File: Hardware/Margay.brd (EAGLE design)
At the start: 50.2 x 30.4 mm, 71 parts, among them IC1 ATMEGA644M, J1 CONN_42.54_SCREW, J2 CONN_6SCREW_2.54, Q1 FDN360P, Q2 DMG3404, Q3 2N7002, Q4 FDN360P, Q6 FDN360P, U2 FT231X-Q

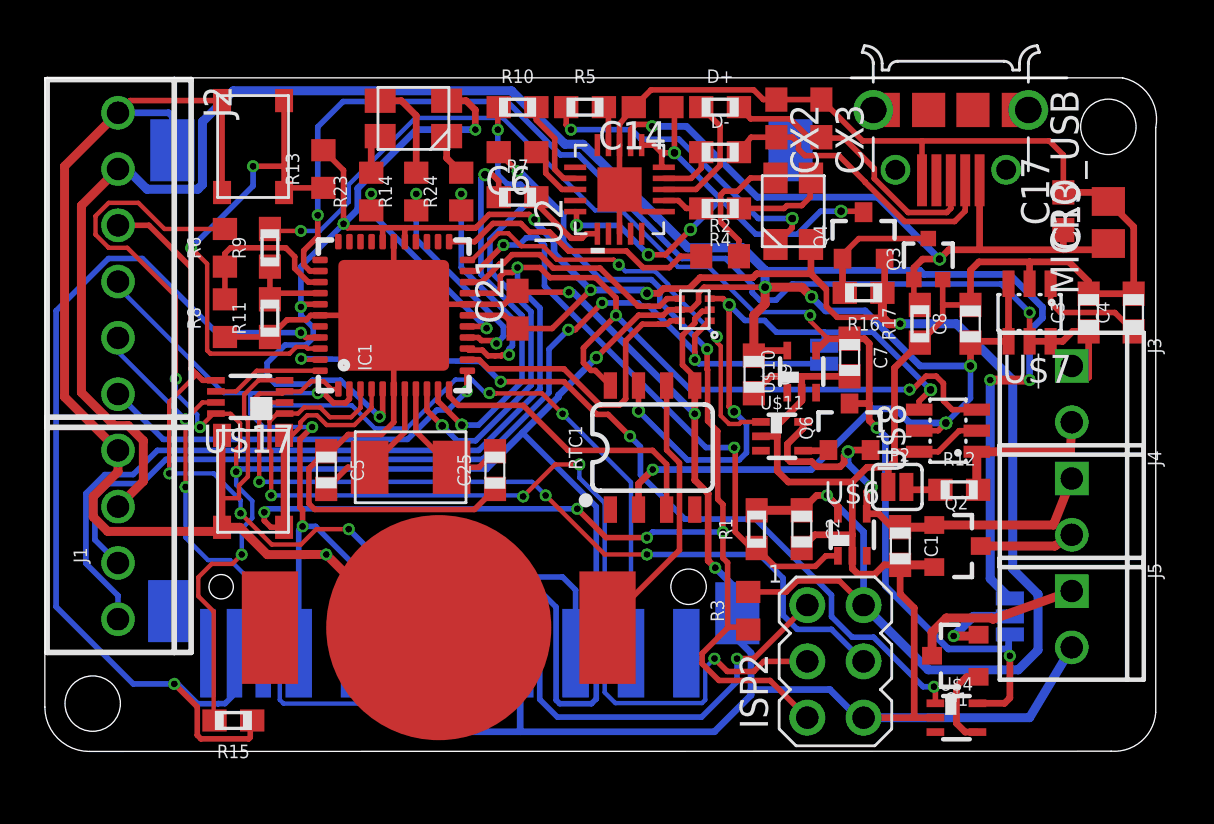
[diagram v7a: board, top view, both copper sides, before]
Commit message: Updated board to account for part changes
Fixed issue where 2x1 connectors displaced, also updated passives to new sizes
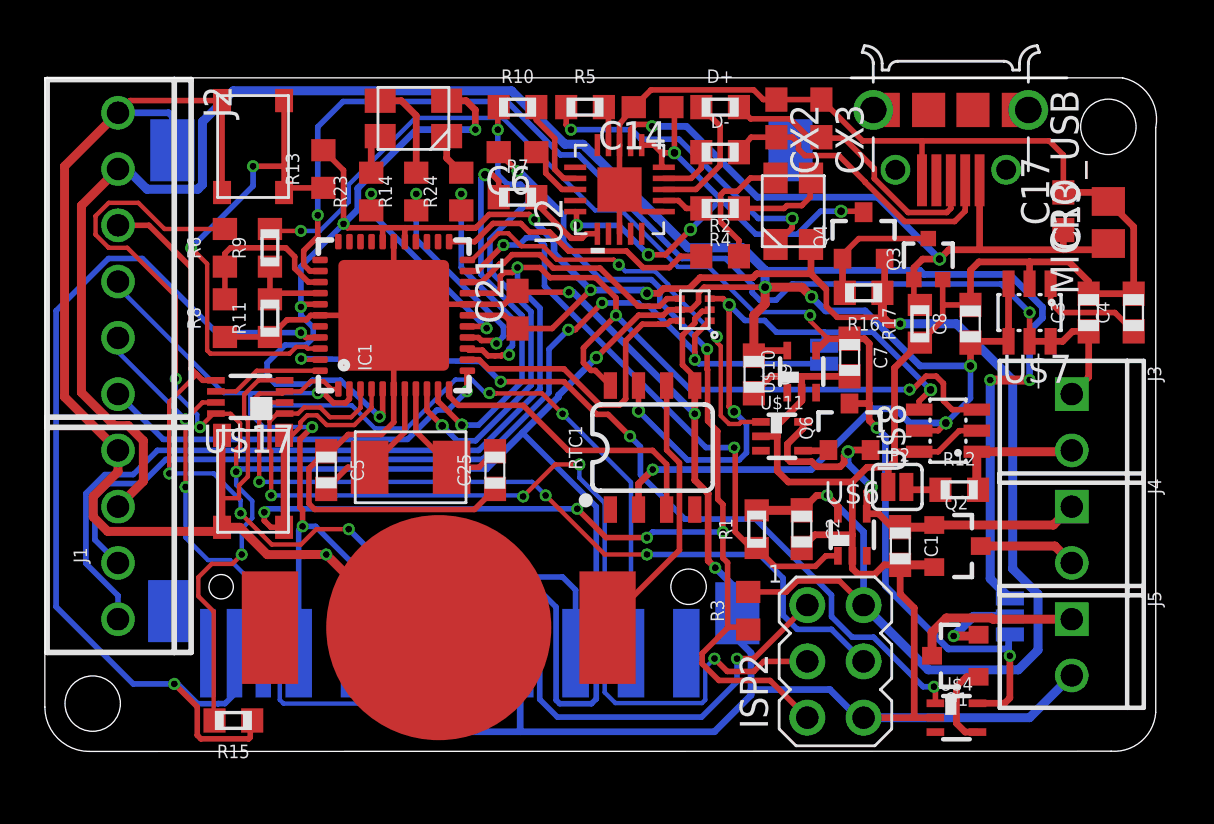
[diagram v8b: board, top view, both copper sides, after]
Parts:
- moved J3 1.27 mm to (46.4, 14.9)
- moved J5 1.27 mm to (46.4, 4.70)
- moved J4 1.27 mm to (46.4, 9.78)
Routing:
- net A0: track 7.30 -> 6.05 mm
- net VBAT+: track 20.9 -> 19.8 mm
- net GND: track 283.6 -> 282.6 mm
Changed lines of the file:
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@@
 <?xml version="1.0" encoding="utf-8"?>
 <!DOCTYPE eagle SYSTEM "eagle.dtd">
-<eagle version="8.5.1">
+<eagle version="9.0.1">
 <drawing>
 <settings>
@@
 <attribute name="MPN" value="OSTVN06A150" x="3.302" y="22.479" size="1.778" layer="27" rot="R270" display="off"/>
 </element>
-<element name="J3" library="bschulz" package="1X02_2.54_SCREWTERM" value="" x="46.355" y="16.129" rot="R270">
-<attribute name="DIGIKEY" value="ED10561-ND" x="46.355" y="16.129" size="1.778" layer="27" rot="R270" display="off"/>
-<attribute name="MF" value="OnShore" x="46.355" y="16.129" size="1.778" layer="27" rot="R270" display="off"/>
-<attribute name="MPN" value="OSTVN02A150" x="46.355" y="16.129" size="1.778" layer="27" rot="R270" display="off"/>
-</element>
-<element name="J4" library="bschulz" package="1X02_2.54_SCREWTERM" value="" x="46.355" y="11.049" rot="R270">
-<attribute name="DIGIKEY" value="ED10561-ND" x="46.355" y="11.049" size="1.778" layer="27" rot="R270" display="off"/>
-<attribute name="MF" value="OnShore" x="46.355" y="11.049" size="1.778" layer="27" rot="R270" display="off"/>
-<attribute name="MPN" value="OSTVN02A150" x="46.355" y="11.049" size="1.778" layer="27" rot="R270" display="off"/>
-</element>
-<element name="J5" library="bschulz" package="1X02_2.54_SCREWTERM" value="" x="46.355" y="5.969" rot="R270">
-<attribute name="DIGIKEY" value="ED10561-ND" x="46.355" y="5.969" size="1.778" layer="27" rot="R270" display="off"/>
-<attribute name="MF" value="OnShore" x="46.355" y="5.969" size="1.778" layer="27" rot="R270" display="off"/>
-<attribute name="MPN" value="OSTVN02A150" x="46.355" y="5.969" size="1.778" layer="27" rot="R270" display="off"/>
+<element name="J3" library="bschulz" package="1X02_2.54_SCREWTERM" value="" x="46.355" y="14.859" rot="R270">
+<attribute name="DIGIKEY" value="ED10561-ND" x="46.355" y="14.859" size="1.778" layer="27" rot="R270" display="off"/>
+<attribute name="MF" value="OnShore" x="46.355" y="14.859" size="1.778" layer="27" rot="R270" display="off"/>
+<attribute name="MPN" value="OSTVN02A150" x="46.355" y="14.859" size="1.778" layer="27" rot="R270" display="off"/>
+</element>
+<element name="J4" library="bschulz" package="1X02_2.54_SCREWTERM" value="" x="46.355" y="9.779" rot="R270">
+<attribute name="DIGIKEY" value="ED10561-ND" x="46.355" y="9.779" size="1.778" layer="27" rot="R270" display="off"/>
+<attribute name="MF" value="OnShore" x="46.355" y="9.779" size="1.778" layer="27" rot="R270" display="off"/>
+<attribute name="MPN" value="OSTVN02A150" x="46.355" y="9.779" size="1.778" layer="27" rot="R270" display="off"/>
+</element>
+<element name="J5" library="bschulz" package="1X02_2.54_SCREWTERM" value="" x="46.355" y="4.699" rot="R270">
+<attribute name="DIGIKEY" value="ED10561-ND" x="46.355" y="4.699" size="1.778" layer="27" rot="R270" display="off"/>
+<attribute name="MF" value="OnShore" x="46.355" y="4.699" size="1.778" layer="27" rot="R270" display="off"/>
+<attribute name="MPN" value="OSTVN02A150" x="46.355" y="4.699" size="1.778" layer="27" rot="R270" display="off"/>
 </element>
 <element name="JP1" library="SparkFun-Jumpers" library_urn="urn:adsk.eagle:library:528" package="SMT-JUMPER_3_1-NC_PASTE_SILK" package3d_urn="urn:adsk.eagle:package:39293/1" value="JUMPER-SMT_3_1-NC_PASTE_SILK" x="43.561" y="6.096" rot="MR270"/>
@@
 <wire x1="36.449" y1="9.779" x2="36.449" y2="12.16115" width="0.3048" layer="1"/>
 <wire x1="38.0746" y1="12.827" x2="38.0746" y2="11.938" width="0.3048" layer="1"/>
-<wire x1="46.355" y1="4.699" x2="44.45" y2="1.524" width="0.4064" layer="16"/>
+<wire x1="46.355" y1="3.429" x2="44.45" y2="1.524" width="0.4064" layer="16"/>
 <wire x1="44.45" y1="1.524" x2="36.957" y2="1.524" width="0.4064" layer="16"/>
 <wire x1="49.403" y1="20.916" x2="49.149" y2="20.662" width="0.254" layer="1"/>
@@
 <wire x1="40.048" y1="10.121" x2="38.608" y2="10.121" width="0.4064" layer="1"/>
 <wire x1="40.3424" y1="10.0266" x2="40.148" y2="10.221" width="0.4064" layer="1"/>
-<wire x1="46.355" y1="12.319" x2="45.527" y2="10.221" width="0.4064" layer="1"/>
+<wire x1="46.355" y1="11.049" x2="45.527" y2="10.221" width="0.4064" layer="1"/>
 <wire x1="45.527" y1="10.221" x2="40.148" y2="10.221" width="0.4064" layer="1"/>
 <contactref element="U$11" pad="5"/>
@@
 <wire x1="40.048" y1="4.318" x2="40.048" y2="5.377" width="0.4064" layer="1"/>
 <wire x1="42.74529375" y1="6.0236" x2="42.79989375" y2="5.969" width="0.4064" layer="1"/>
-<wire x1="42.79989375" y1="5.969" x2="46.355" y2="7.239" width="0.4064" layer="1"/>
+<wire x1="42.79989375" y1="5.969" x2="46.355" y2="5.969" width="0.4064" layer="1"/>
 <wire x1="40.048" y1="5.377" x2="40.6946" y2="6.0236" width="0.4064" layer="1"/>
 <wire x1="40.6946" y1="6.0236" x2="42.74529375" y2="6.0236" width="0.4064" layer="1"/>
@@
 <wire x1="44.45" y1="19.812" x2="43.1602" y2="21.1018" width="0.254" layer="16"/>
 <wire x1="43.1602" y1="21.1018" x2="33.734375" y2="21.1018" width="0.254" layer="16"/>
-<wire x1="46.355" y1="17.399" x2="47.117" y2="16.891" width="0.3048" layer="1"/>
+<wire x1="46.355" y1="16.129" x2="47.117" y2="16.891" width="0.3048" layer="1"/>
 <wire x1="47.117" y1="16.891" x2="47.117" y2="18.962" width="0.3048" layer="1"/>
 <wire x1="45.4" y1="18.512" x2="45.944" y2="18.512" width="0.3048" layer="1"/>
@@
 <wire x1="42.067" y1="11.869" x2="42.125" y2="11.811" width="0.4064" layer="1"/>
 <wire x1="42.067" y1="13.528" x2="46.294" y2="13.528" width="0.4064" layer="1"/>
-<wire x1="46.294" y1="13.528" x2="46.355" y2="14.859" width="0.4064" layer="1"/>
+<wire x1="46.294" y1="13.528" x2="46.355" y2="13.589" width="0.4064" layer="1"/>
 </signal>
 <signal name="VBAT-">
 <contactref element="Q2" pad="3"/>
 <contactref element="J4" pad="P1"/>
-<wire x1="46.355" y1="9.779" x2="45.593" y2="9.271" width="0.4064" layer="1"/>
+<wire x1="46.355" y1="8.509" x2="45.593" y2="9.271" width="0.4064" layer="1"/>
 <wire x1="45.593" y1="9.271" x2="42.248" y2="9.271" width="0.4064" layer="1"/>
 </signal>
